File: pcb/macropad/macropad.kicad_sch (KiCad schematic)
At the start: 7 parts, among them SW1 SW_Push, SW2 SW_Push, SW3 SW_Push, SW4 SW_Push, U1 XIAO-RP2040-DIP

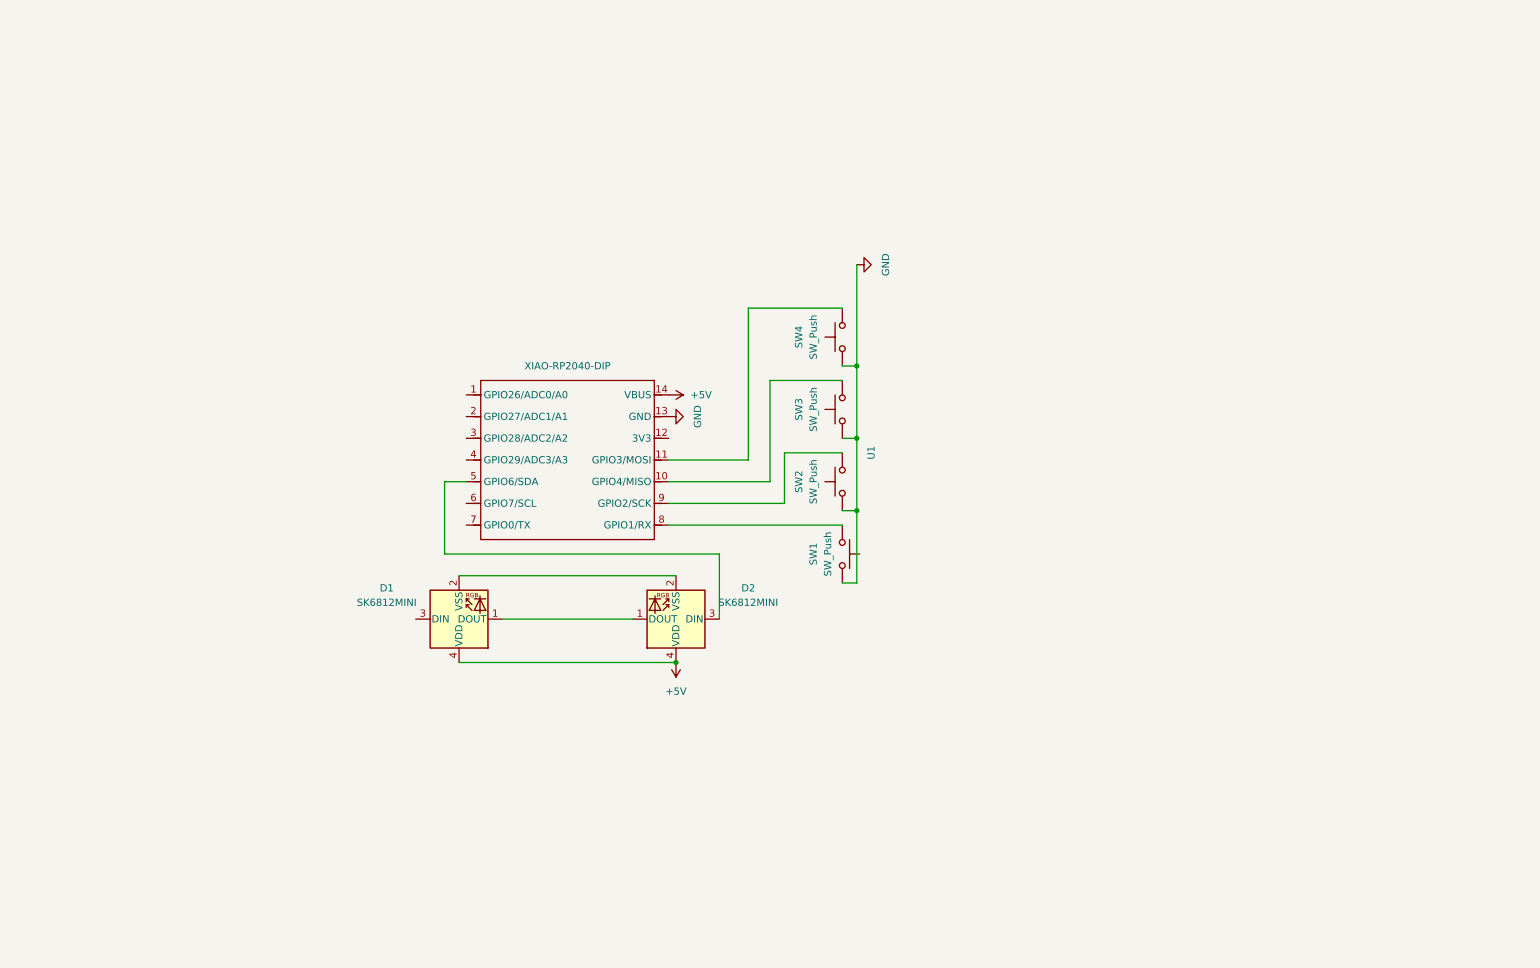
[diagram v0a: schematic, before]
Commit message: changes to the pcb, case changes will follow
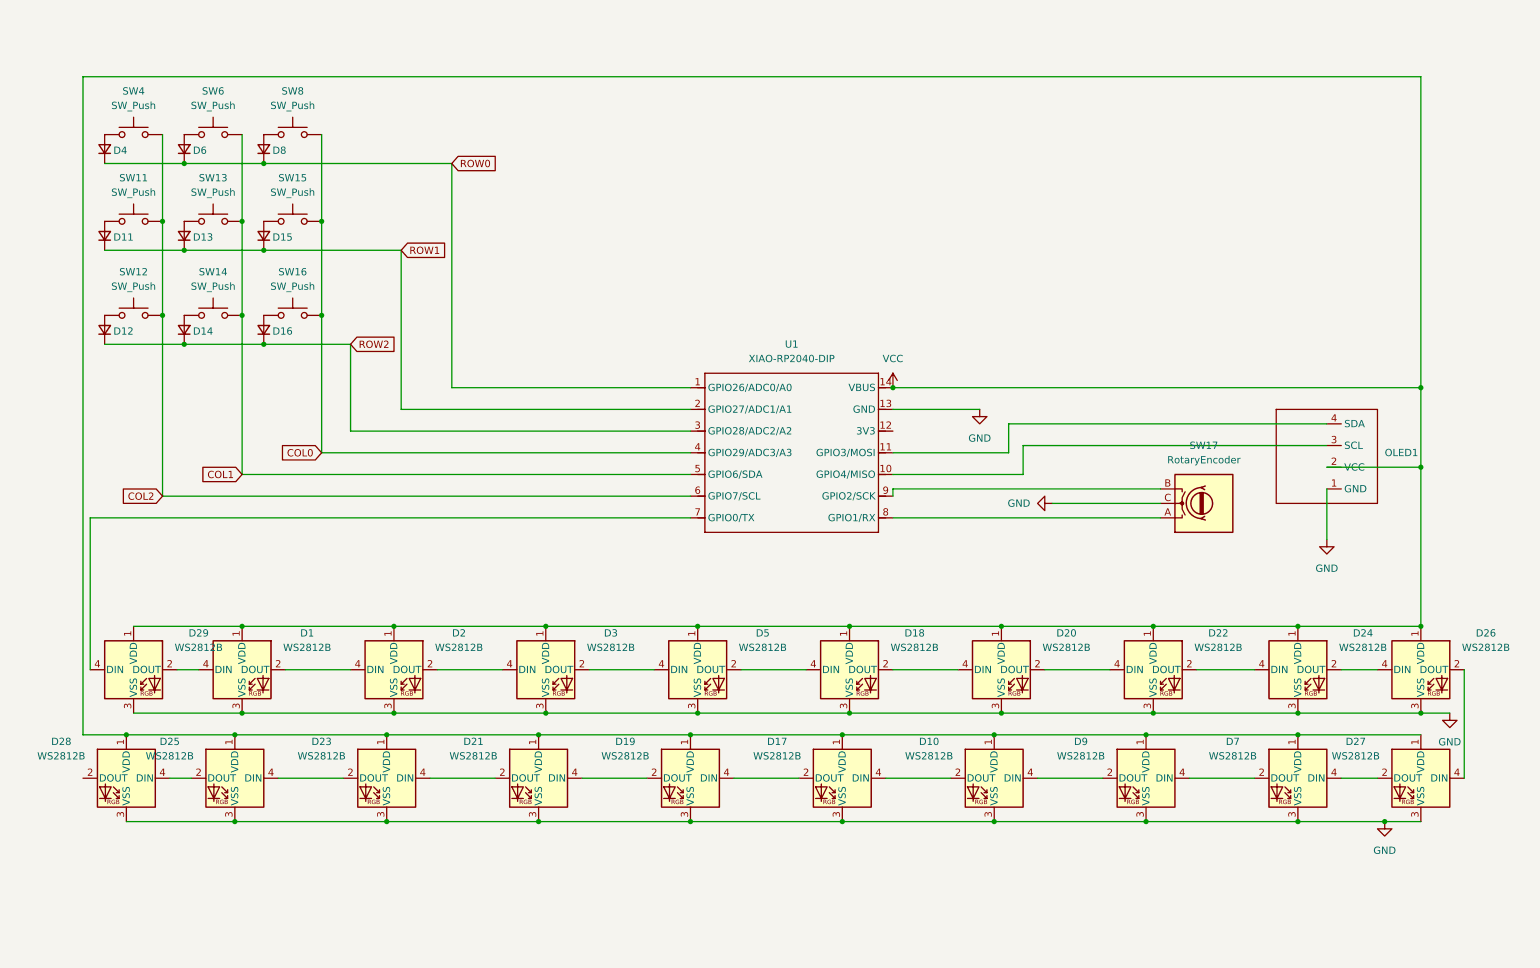
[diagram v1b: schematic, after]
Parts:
- removed D1, D2: SK6812MINI, LED_SMD:LED_SK6812MINI_PLCC4_3.5x3.5mm_P1.75mm, symbol LED:SK6812MINI
- removed SW1, SW2, SW3: SW_Push, Button_Switch_Keyboard:SW_Cherry_MX_1.00u_PCB, symbol Switch:SW_Push
- added D1, D10, D17, D18, D19, D2, D20, D21, D22, D23, D24, D25, D26, D27, D28, D29, D3, D5, D7, D9: WS2812B, LED_SMD:LED_WS2812B_PLCC4_5.0x5.0mm_P3.2mm, symbol LED:WS2812B
- added D11, D12, D13, D14, D15, D16, D4, D6, D8: D_Small, Diode_THT:D_5W_P5.08mm_Vertical_AnodeUp, symbol Device:D_Small
- added OLED1: ~, Downloads:SSD1306-0.91-OLED-4pin-128x32, symbol OLED:OLED
- added SW11, SW12, SW13, SW14, SW15, SW16, SW6, SW8: SW_Push, Button_Switch_Keyboard:SW_Cherry_MX_1.00u_PCB, symbol Switch:SW_Push
- added SW17: RotaryEncoder, Downloads:RotaryEncoder_Alps_EC11E_Vertical_H20mm, symbol Device:RotaryEncoder
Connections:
- net GND: now also D1.3 (VSS), D10.3 (VSS), D17.3 (VSS), D18.3 (VSS), D19.3 (VSS), D2.3 (VSS), D20.3 (VSS), D21.3 (VSS), D22.3 (VSS), D23.3 (VSS), D24.3 (VSS), D25.3 (VSS), D26.3 (VSS), D27.3 (VSS), D28.3 (VSS), D29.3 (VSS), D3.3 (VSS), D5.3 (VSS), D7.3 (VSS), D9.3 (VSS), OLED1.1 (GND), SW17.C; no longer SW4.1
- net at U1.10 (GPIO4/MISO): now also OLED1.3 (SCL)
- net at U1.11 (GPIO3/MOSI): now also OLED1.4 (SDA); no longer SW4.2
- net COL1: now reaches U1.5 (GPIO6/SDA)
- net COL1: now also SW13.2, SW14.2, SW6.2
- net at U1.9 (GPIO2/SCK): now also SW17.B
- net at U1.8 (GPIO1/RX): now also SW17.A
- net ROW0: now reaches U1.1 (GPIO26/ADC0/A0)
- net ROW0: now also D4.1 (K), D6.1 (K), D8.1 (K)
- net ROW1: now reaches U1.2 (GPIO27/ADC1/A1)
- net ROW1: now also D11.1 (K), D13.1 (K), D15.1 (K)
- net ROW2: now reaches U1.3 (GPIO28/ADC2/A2)
- net ROW2: now also D12.1 (K), D14.1 (K), D16.1 (K)
- net COL0: now reaches U1.4 (GPIO29/ADC3/A3)
- net COL0: now also SW15.2, SW16.2, SW8.2
- net COL2: now reaches U1.6 (GPIO7/SCL)
- net COL2: now also SW4.2, SW11.2, SW12.2
- net at U1.7 (GPIO0/TX): now also D29.4 (DIN)
- net +5V renamed VCC
- net VCC: now also D1.1 (VDD), D10.1 (VDD), D17.1 (VDD), D18.1 (VDD), D19.1 (VDD), D2.1 (VDD), D20.1 (VDD), D21.1 (VDD), D22.1 (VDD), D23.1 (VDD), D24.1 (VDD), D25.1 (VDD), D26.1 (VDD), D27.1 (VDD), D28.1 (VDD), D29.1 (VDD), D3.1 (VDD), D5.1 (VDD), D7.1 (VDD), D9.1 (VDD), OLED1.2 (VCC)
- new net: D12.2 (A), SW12.1
- new net: D20.2 (DOUT), D22.4 (DIN)
- new net: D18.2 (DOUT), D20.4 (DIN)
- new net: D18.4 (DIN), D5.2 (DOUT)
- new net: D2.2 (DOUT), D3.4 (DIN)
- new net: D1.2 (DOUT), D2.4 (DIN)
- new net: D6.2 (A), SW6.1
- new net: D14.2 (A), SW14.1
- new net: D7.2 (DOUT), D9.4 (DIN)
- new net: D27.2 (DOUT), D7.4 (DIN)
- new net: D4.2 (A), SW4.1
- new net: D19.2 (DOUT), D21.4 (DIN)
- new net: D17.2 (DOUT), D19.4 (DIN)
- new net: D21.2 (DOUT), D23.4 (DIN)
- new net: D13.2 (A), SW13.1
- new net: D11.2 (A), SW11.1
- new net: D22.2 (DOUT), D24.4 (DIN)
- new net: D10.2 (DOUT), D17.4 (DIN)
- new net: D10.4 (DIN), D9.2 (DOUT)
- new net: D16.2 (A), SW16.1
- new net: D1.4 (DIN), D29.2 (DOUT)
- new net: D25.2 (DOUT), D28.4 (DIN)
- new net: D15.2 (A), SW15.1
- new net: D26.2 (DOUT), D27.4 (DIN)
- new net: D24.2 (DOUT), D26.4 (DIN)
- new net: D8.2 (A), SW8.1
- new net: D23.2 (DOUT), D25.4 (DIN)
- new net: D3.2 (DOUT), D5.4 (DIN)

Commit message: remade pcb
removed leds and better wiring (much better)
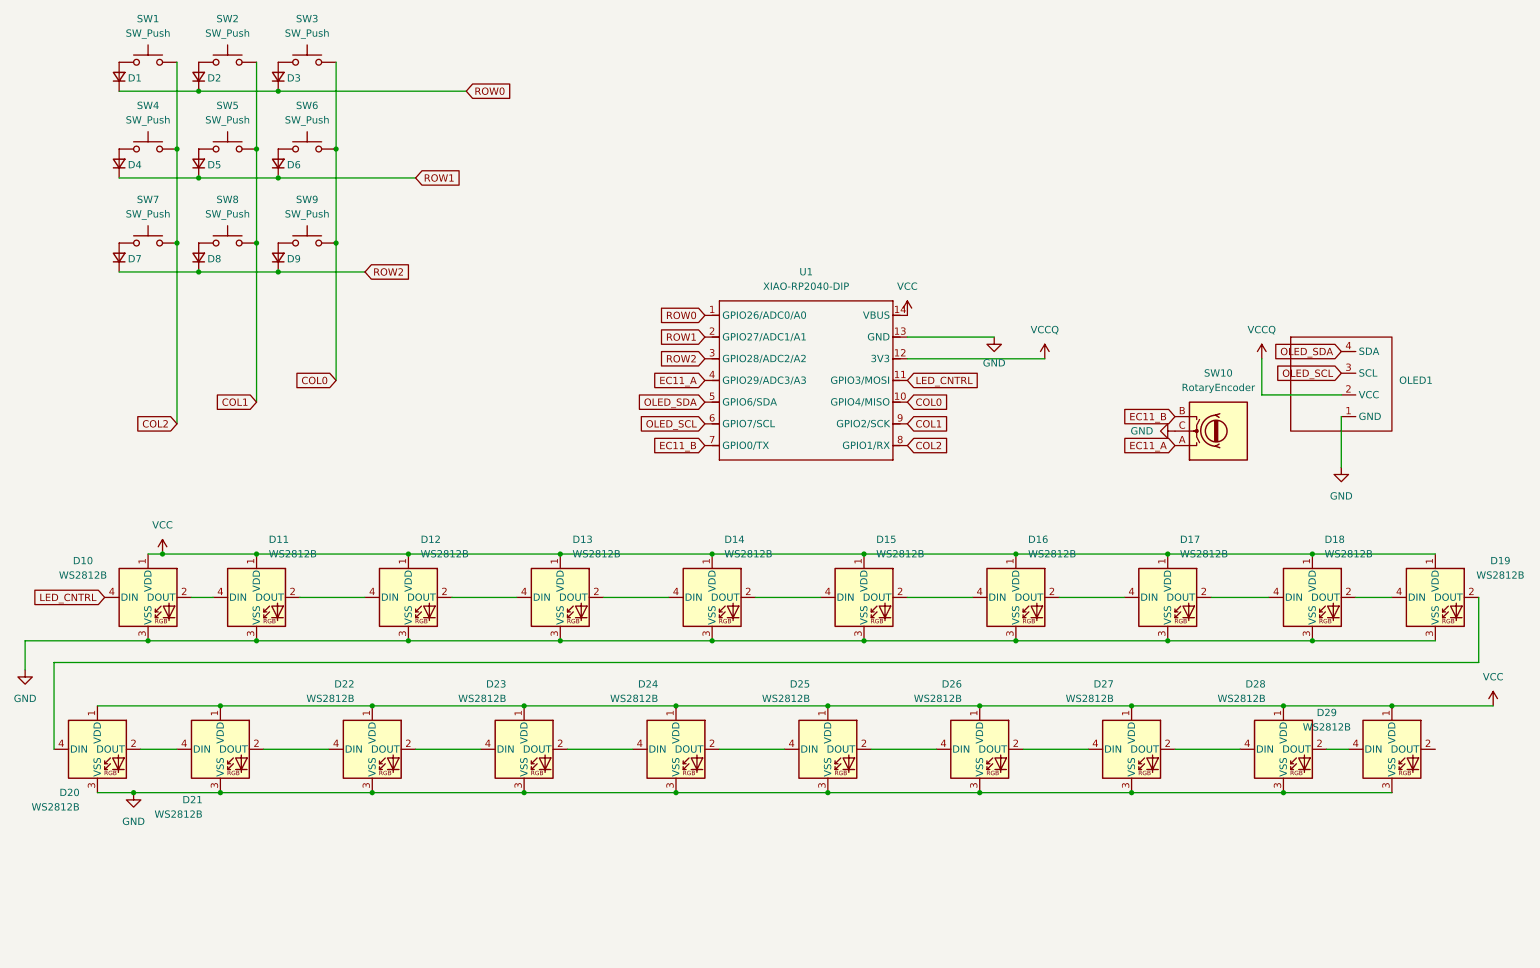
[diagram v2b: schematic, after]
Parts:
- SW1: renamed from SW4; footprint Button_Switch_Keyboard:SW_Cherry_MX_1.00u_PCB -> Library:SW_Cherry_MX_1.00u_PCB
- SW2: renamed from SW6; footprint Button_Switch_Keyboard:SW_Cherry_MX_1.00u_PCB -> Library:SW_Cherry_MX_1.00u_PCB
- SW3: renamed from SW8; footprint Button_Switch_Keyboard:SW_Cherry_MX_1.00u_PCB -> Library:SW_Cherry_MX_1.00u_PCB
- SW4: renamed from SW11; footprint Button_Switch_Keyboard:SW_Cherry_MX_1.00u_PCB -> Library:SW_Cherry_MX_1.00u_PCB
- SW5: renamed from SW13; footprint Button_Switch_Keyboard:SW_Cherry_MX_1.00u_PCB -> Library:SW_Cherry_MX_1.00u_PCB
- SW6: renamed from SW15; footprint Button_Switch_Keyboard:SW_Cherry_MX_1.00u_PCB -> Library:SW_Cherry_MX_1.00u_PCB
- SW7: renamed from SW12; footprint Button_Switch_Keyboard:SW_Cherry_MX_1.00u_PCB -> Library:SW_Cherry_MX_1.00u_PCB
- SW8: renamed from SW14; footprint Button_Switch_Keyboard:SW_Cherry_MX_1.00u_PCB -> Library:SW_Cherry_MX_1.00u_PCB
- SW9: renamed from SW16; footprint Button_Switch_Keyboard:SW_Cherry_MX_1.00u_PCB -> Library:SW_Cherry_MX_1.00u_PCB
- renumbered D4 to D1, D29 to D10, D1 to D11, D2 to D12, D3 to D13, D5 to D14, D18 to D15, D20 to D16, D22 to D17, D24 to D18, D26 to D19, D6 to D2, D27 to D20, D7 to D21, D9 to D22, D10 to D23, D17 to D24, D19 to D25, D21 to D26, D23 to D27, D25 to D28, D28 to D29, D8 to D3, D11 to D4, D13 to D5, D15 to D6, D12 to D7, D14 to D8, D16 to D9, SW17 to SW10
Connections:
- net COL0: now also U1.10 (GPIO4/MISO); no longer U1.4 (GPIO29/ADC3/A3)
- net COL1: now also U1.9 (GPIO2/SCK); no longer U1.5 (GPIO6/SDA)
- net COL2: now also U1.8 (GPIO1/RX); no longer U1.6 (GPIO7/SCL)
- net VCC: no longer OLED1.2 (VCC)
- net EC11_A: now reaches SW10.A
- net EC11_A: now also U1.4 (GPIO29/ADC3/A3); no longer U1.8 (GPIO1/RX)
- net EC11_B: now reaches SW10.B
- net EC11_B: now also U1.7 (GPIO0/TX); no longer U1.9 (GPIO2/SCK)
- net OLED_SCL: now reaches OLED1.3 (SCL)
- net OLED_SCL: now also U1.6 (GPIO7/SCL); no longer U1.10 (GPIO4/MISO)
- net LED_CNTRL: now reaches U1.11 (GPIO3/MOSI)
- net LED_CNTRL: now also D10.4 (DIN); no longer OLED1.4 (SDA)
- net VCCQ: now reaches U1.12 (3V3)
- net VCCQ: now also OLED1.2 (VCC)
- new net OLED_SDA: OLED1.4 (SDA), U1.5 (GPIO6/SDA)
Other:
- moved on the sheet: D1, D10, D11, D12, D13, D14, D15, D16, D17, D18, D19, D2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

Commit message: added leds
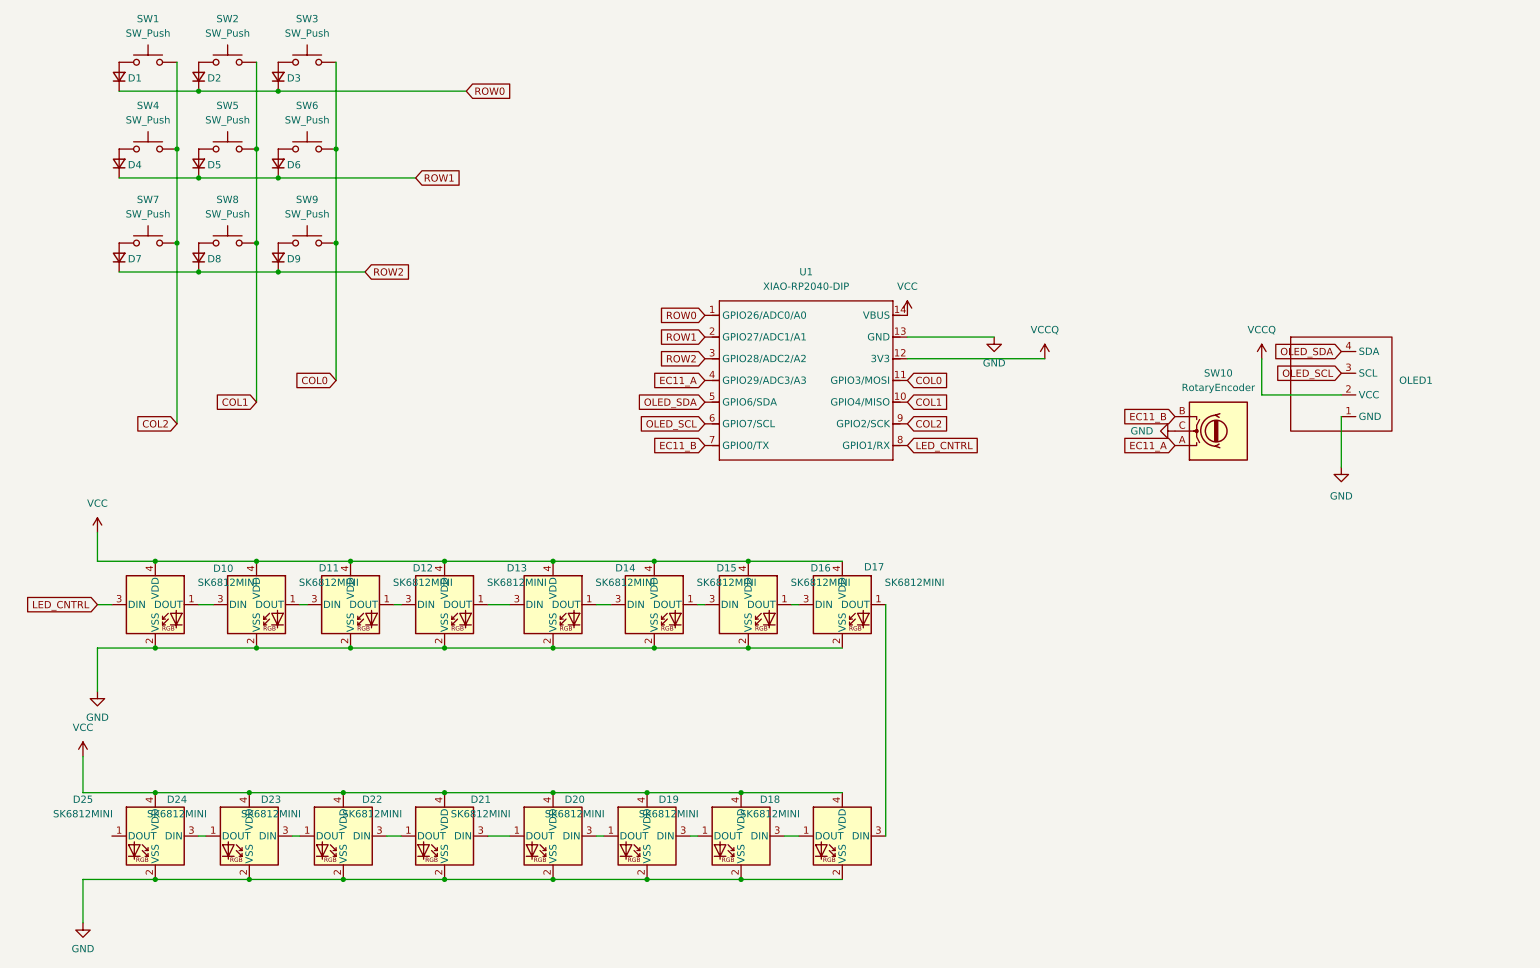
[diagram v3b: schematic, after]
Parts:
- removed D10, D11, D12, D13, D14, D15, D16, D17, D18, D19, D20, D21, D22, D23, D24, D25, D26, D27, D28, D29: WS2812B, LED_SMD:LED_WS2812B_PLCC4_5.0x5.0mm_P3.2mm, symbol LED:WS2812B
- added D10, D11, D12, D13, D14, D15, D16, D17, D18, D19, D20, D21, D22, D23, D24, D25: SK6812MINI, Downloads:SK6812-MINI-E, symbol LED:SK6812MINI
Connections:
- net COL0: now also U1.11 (GPIO3/MOSI); no longer U1.10 (GPIO4/MISO)
- net COL1: now also U1.10 (GPIO4/MISO); no longer U1.9 (GPIO2/SCK)
- net COL2: now also U1.9 (GPIO2/SCK); no longer U1.8 (GPIO1/RX)
- net GND: now also D10.2 (VSS), D11.2 (VSS), D12.2 (VSS), D13.2 (VSS), D14.2 (VSS), D15.2 (VSS), D16.2 (VSS), D17.2 (VSS), D18.2 (VSS), D19.2 (VSS), D20.2 (VSS), D21.2 (VSS), D22.2 (VSS), D23.2 (VSS), D24.2 (VSS), D25.2 (VSS)
- net LED_CNTRL: now also U1.8 (GPIO1/RX), D10.3 (DIN); no longer U1.11 (GPIO3/MOSI)
- net VCC: now also D10.4 (VDD), D11.4 (VDD), D12.4 (VDD), D13.4 (VDD), D14.4 (VDD), D15.4 (VDD), D16.4 (VDD), D17.4 (VDD), D18.4 (VDD), D19.4 (VDD), D20.4 (VDD), D21.4 (VDD), D22.4 (VDD), D23.4 (VDD), D24.4 (VDD), D25.4 (VDD)
- new net: D20.1 (DOUT), D21.3 (DIN)
- new net: D19.1 (DOUT), D20.3 (DIN)
- new net: D16.1 (DOUT), D17.3 (DIN)
- new net: D15.1 (DOUT), D16.3 (DIN)
- new net: D21.1 (DOUT), D22.3 (DIN)
- new net: D24.1 (DOUT), D25.3 (DIN)
- new net: D11.1 (DOUT), D12.3 (DIN)
- new net: D10.1 (DOUT), D11.3 (DIN)
- new net: D13.1 (DOUT), D14.3 (DIN)
- new net: D12.1 (DOUT), D13.3 (DIN)
- new net: D23.1 (DOUT), D24.3 (DIN)
- new net: D22.1 (DOUT), D23.3 (DIN)
- new net: D17.1 (DOUT), D18.3 (DIN)
- new net: D18.1 (DOUT), D19.3 (DIN)
- new net: D14.1 (DOUT), D15.3 (DIN)

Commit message: added the ec11 as a switch and some extra organization
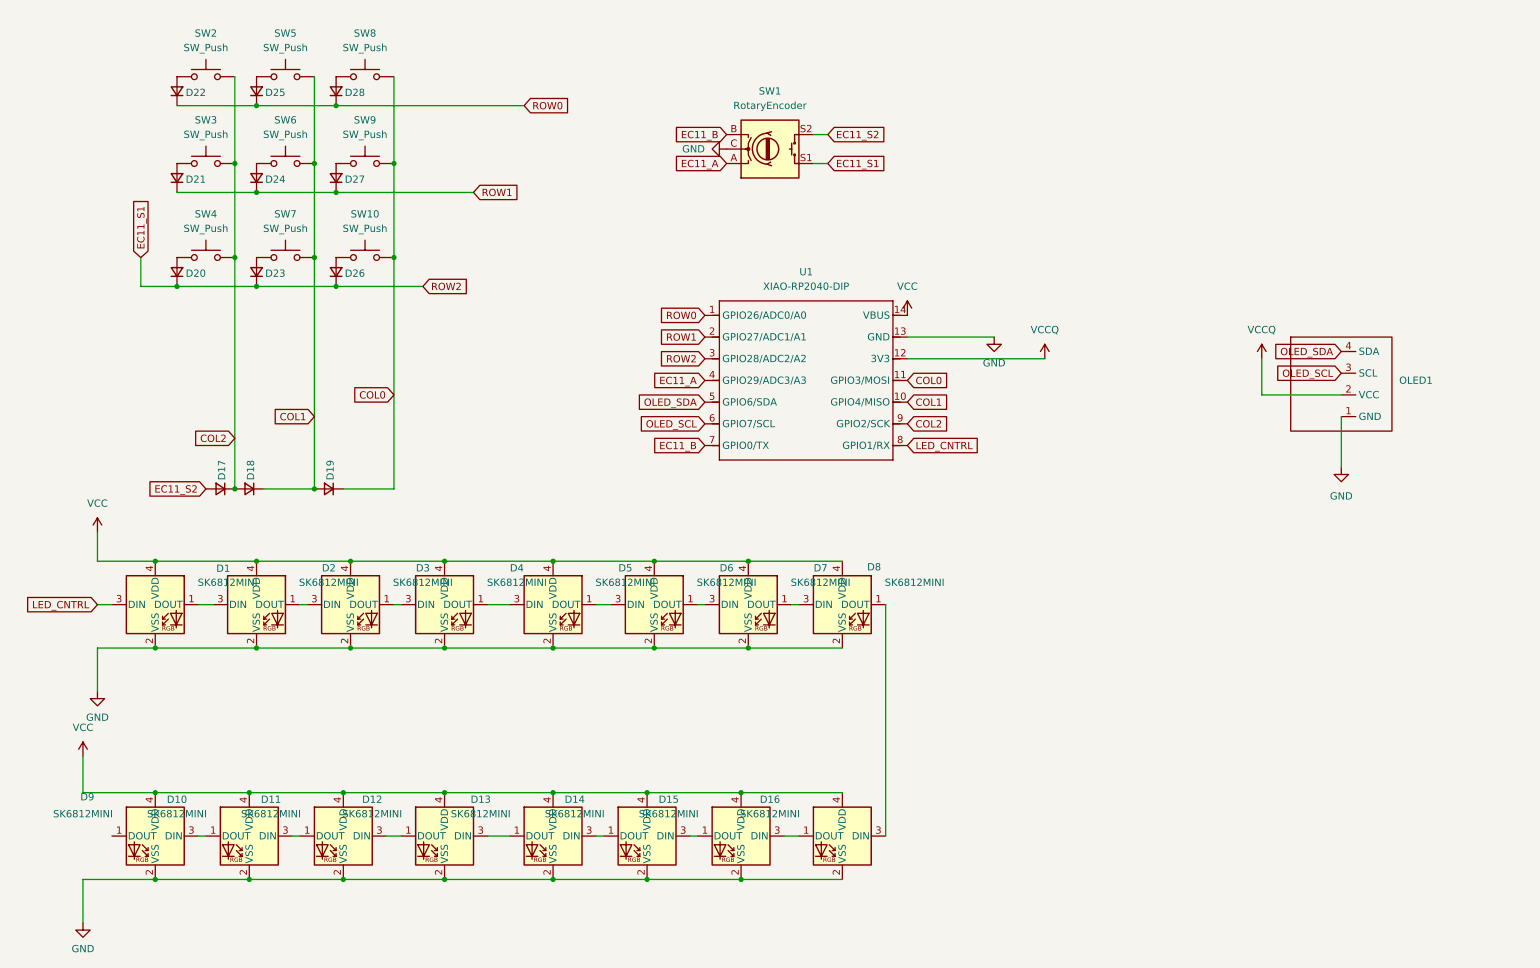
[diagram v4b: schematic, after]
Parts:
- added D17, D18, D19: D_Small, Diode_THT:D_5W_P5.08mm_Vertical_AnodeUp, symbol Device:D_Small
- SW1: renamed from SW10; footprint Downloads:RotaryEncoder_Alps_EC11E_Vertical_H20mm -> Rotary_Encoder:RotaryEncoder_Alps_EC11E-Switch_Vertical_H20mm; symbol Device:RotaryEncoder -> Device:RotaryEncoder_Switch
- renumbered D10 to D1, D24 to D10, D23 to D11, D22 to D12, D21 to D13, D20 to D14, D19 to D15, D18 to D16, D11 to D2, D7 to D20, D4 to D21, D1 to D22, D8 to D23, D5 to D24, D2 to D25, D9 to D26, D6 to D27, D3 to D28, D12 to D3, D13 to D4, D14 to D5, D15 to D6, D16 to D7, D17 to D8, D25 to D9, SW9 to SW10, SW1 to SW2, SW4 to SW3, SW7 to SW4, SW2 to SW5, SW5 to SW6, SW8 to SW7, SW3 to SW8, SW6 to SW9
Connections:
- net COL0: now also D19.1 (K)
- net COL1: now also D18.1 (K), D19.2 (A)
- net COL2: now also D17.1 (K), D18.2 (A)
- net ROW2 renamed EC11_S1
- net EC11_S1: now also SW1.S1
- new net EC11_S2: D17.2 (A), SW1.S2
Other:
- moved on the sheet: D20, D21, D22, D23, D24, D25, D26, D27, D28, SW10, SW2, SW3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
